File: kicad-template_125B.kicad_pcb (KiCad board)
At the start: 2 copper layers, 60 x 80 mm, 3 parts, among them J1 Barrel_Jack_Switch, J2 AudioJack_TRS, J3 AudioJack_TRS

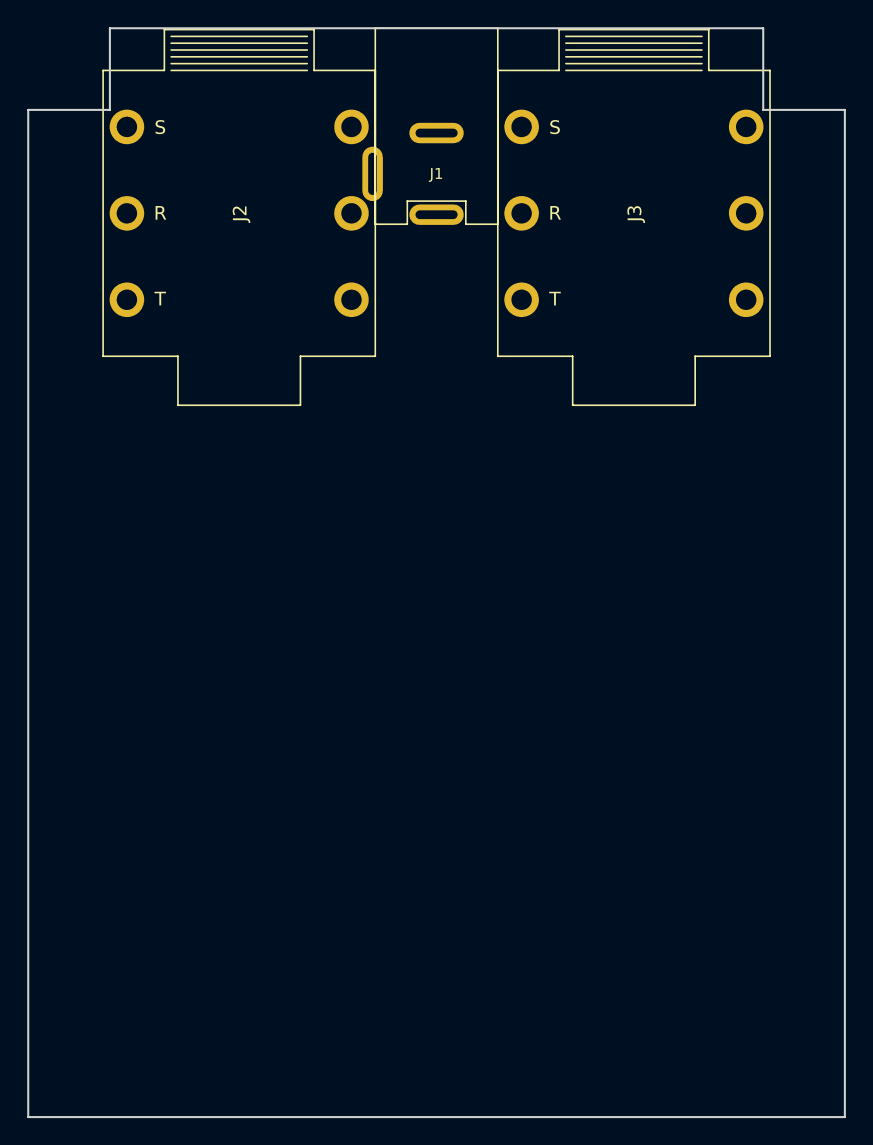
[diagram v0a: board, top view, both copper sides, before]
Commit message: Added jacks to schematic, filetted 125B PCB
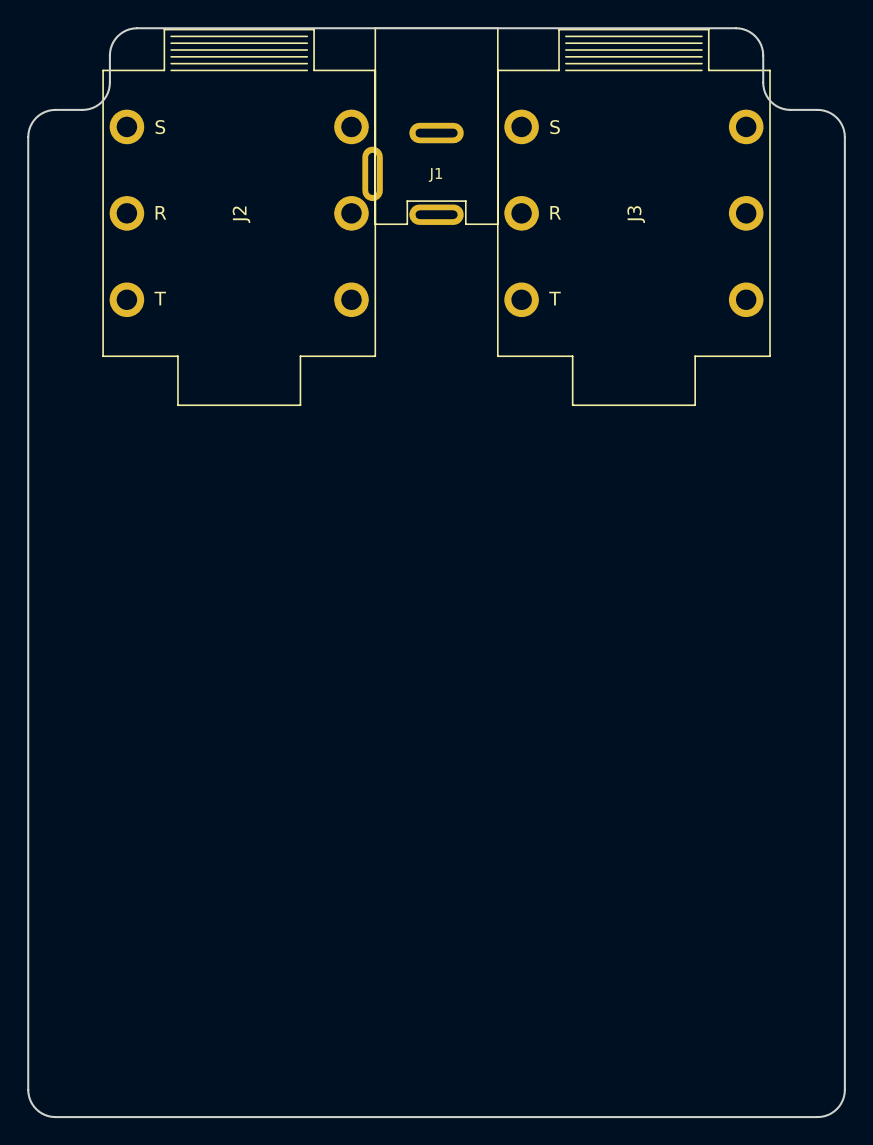
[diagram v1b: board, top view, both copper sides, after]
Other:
- outline, holes or cut-outs redrawn
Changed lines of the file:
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@@
   (general
     (thickness 1.6)
-    (drawings 36)
+    (drawings 44)
     (tracks 0)
     (zones 0)
@@
       (effects (font (size 1 1) (thickness 0.15)))
     )
+    (fp_line (start -2.15 12.7) (end -2.15 14.4) (layer F.SilkS) (width 0.12))
+    (fp_line (start 2.15 12.7) (end -2.15 12.7) (layer F.SilkS) (width 0.12))
+    (fp_line (start 2.15 14.4) (end 2.15 12.7) (layer F.SilkS) (width 0.12))
+    (fp_line (start 2.15 14.4) (end 4.5 14.4) (layer F.SilkS) (width 0.12))
+    (fp_line (start -4.5 0) (end -4.5 14.4) (layer F.SilkS) (width 0.12))
+    (fp_line (start -4.5 14.4) (end -2.15 14.4) (layer F.SilkS) (width 0.12))
+    (fp_line (start 4.5 0) (end 4.5 14.4) (layer F.SilkS) (width 0.12))
     (fp_line (start -4.5 0) (end 4.5 0) (layer F.SilkS) (width 0.12))
-    (fp_line (start 4.5 0) (end 4.5 14.4) (layer F.SilkS) (width 0.12))
-    (fp_line (start -4.5 14.4) (end -2.15 14.4) (layer F.SilkS) (width 0.12))
-    (fp_line (start -4.5 0) (end -4.5 14.4) (layer F.SilkS) (width 0.12))
-    (fp_line (start 2.15 14.4) (end 4.5 14.4) (layer F.SilkS) (width 0.12))
-    (fp_line (start 2.15 14.4) (end 2.15 12.7) (layer F.SilkS) (width 0.12))
-    (fp_line (start 2.15 12.7) (end -2.15 12.7) (layer F.SilkS) (width 0.12))
-    (fp_line (start -2.15 12.7) (end -2.15 14.4) (layer F.SilkS) (width 0.12))
     (pad 3 thru_hole oval (at -4.7 10.7 180) (size 1.5 4) (drill oval 0.65 3.1) (layers *.Cu *.Mask)
       (net 4 "Net-(J1-Pad3)"))
@@
       (effects (font (size 1 1) (thickness 0.15)))
     )
+    (fp_line (start 10 -10.5) (end 10 10.5) (layer F.SilkS) (width 0.12))
+    (fp_line (start -10 10.5) (end -10 -10.5) (layer F.SilkS) (width 0.12))
+    (fp_line (start -10 10.5) (end -4.5 10.5) (layer F.SilkS) (width 0.12))
+    (fp_line (start -4.5 10.5) (end -4.5 14.1) (layer F.SilkS) (width 0.12))
+    (fp_line (start -4.5 14.1) (end 4.5 14.1) (layer F.SilkS) (width 0.12))
+    (fp_line (start 4.5 14.1) (end 4.5 10.5) (layer F.SilkS) (width 0.12))
+    (fp_line (start 4.5 10.5) (end 10 10.5) (layer F.SilkS) (width 0.12))
+    (fp_line (start 10 -10.5) (end 5.5 -10.5) (layer F.SilkS) (width 0.12))
+    (fp_line (start 5.5 -10.5) (end 5.5 -13.5) (layer F.SilkS) (width 0.12))
+    (fp_line (start 5.5 -13.5) (end -5.5 -13.5) (layer F.SilkS) (width 0.12))
+    (fp_line (start -5.5 -13.5) (end -5.5 -10.5) (layer F.SilkS) (width 0.12))
+    (fp_line (start -5.5 -10.5) (end -10 -10.5) (layer F.SilkS) (width 0.12))
+    (fp_line (start -5 -13) (end 5 -13) (layer F.SilkS) (width 0.12))
+    (fp_line (start 5 -12.5) (end -5 -12.5) (layer F.SilkS) (width 0.12))
+    (fp_line (start -5 -12) (end 5 -12) (layer F.SilkS) (width 0.12))
+    (fp_line (start 5 -11.5) (end -5 -11.5) (layer F.SilkS) (width 0.12))
+    (fp_line (start -5 -11) (end 5 -11) (layer F.SilkS) (width 0.12))
     (fp_line (start 5 -10.5) (end -5 -10.5) (layer F.SilkS) (width 0.12))
-    (fp_line (start -5 -11) (end 5 -11) (layer F.SilkS) (width 0.12))
-    (fp_line (start 5 -11.5) (end -5 -11.5) (layer F.SilkS) (width 0.12))
-    (fp_line (start -5 -12) (end 5 -12) (layer F.SilkS) (width 0.12))
-    (fp_line (start 5 -12.5) (end -5 -12.5) (layer F.SilkS) (width 0.12))
-    (fp_line (start -5 -13) (end 5 -13) (layer F.SilkS) (width 0.12))
-    (fp_line (start -5.5 -10.5) (end -10 -10.5) (layer F.SilkS) (width 0.12))
-    (fp_line (start -5.5 -13.5) (end -5.5 -10.5) (layer F.SilkS) (width 0.12))
-    (fp_line (start 5.5 -13.5) (end -5.5 -13.5) (layer F.SilkS) (width 0.12))
-    (fp_line (start 5.5 -10.5) (end 5.5 -13.5) (layer F.SilkS) (width 0.12))
-    (fp_line (start 10 -10.5) (end 5.5 -10.5) (layer F.SilkS) (width 0.12))
-    (fp_line (start 4.5 10.5) (end 10 10.5) (layer F.SilkS) (width 0.12))
-    (fp_line (start 4.5 14.1) (end 4.5 10.5) (layer F.SilkS) (width 0.12))
-    (fp_line (start -4.5 14.1) (end 4.5 14.1) (layer F.SilkS) (width 0.12))
-    (fp_line (start -4.5 10.5) (end -4.5 14.1) (layer F.SilkS) (width 0.12))
-    (fp_line (start -10 10.5) (end -4.5 10.5) (layer F.SilkS) (width 0.12))
-    (fp_line (start -10 10.5) (end -10 -10.5) (layer F.SilkS) (width 0.12))
-    (fp_line (start 10 -10.5) (end 10 10.5) (layer F.SilkS) (width 0.12))
     (fp_text user R (at -5.8 0) (layer F.SilkS)
       (effects (font (size 1 1) (thickness 0.15)))
@@
       (effects (font (size 1 1) (thickness 0.15)))
     )
+    (fp_line (start 10 -10.5) (end 10 10.5) (layer F.SilkS) (width 0.12))
+    (fp_line (start -10 10.5) (end -10 -10.5) (layer F.SilkS) (width 0.12))
+    (fp_line (start -10 10.5) (end -4.5 10.5) (layer F.SilkS) (width 0.12))
+    (fp_line (start -4.5 10.5) (end -4.5 14.1) (layer F.SilkS) (width 0.12))
+    (fp_line (start -4.5 14.1) (end 4.5 14.1) (layer F.SilkS) (width 0.12))
+    (fp_line (start 4.5 14.1) (end 4.5 10.5) (layer F.SilkS) (width 0.12))
+    (fp_line (start 4.5 10.5) (end 10 10.5) (layer F.SilkS) (width 0.12))
+    (fp_line (start 10 -10.5) (end 5.5 -10.5) (layer F.SilkS) (width 0.12))
+    (fp_line (start 5.5 -10.5) (end 5.5 -13.5) (layer F.SilkS) (width 0.12))
+    (fp_line (start 5.5 -13.5) (end -5.5 -13.5) (layer F.SilkS) (width 0.12))
+    (fp_line (start -5.5 -13.5) (end -5.5 -10.5) (layer F.SilkS) (width 0.12))
+    (fp_line (start -5.5 -10.5) (end -10 -10.5) (layer F.SilkS) (width 0.12))
+    (fp_line (start -5 -13) (end 5 -13) (layer F.SilkS) (width 0.12))
+    (fp_line (start 5 -12.5) (end -5 -12.5) (layer F.SilkS) (width 0.12))
+    (fp_line (start -5 -12) (end 5 -12) (layer F.SilkS) (width 0.12))
+    (fp_line (start 5 -11.5) (end -5 -11.5) (layer F.SilkS) (width 0.12))
+    (fp_line (start -5 -11) (end 5 -11) (layer F.SilkS) (width 0.12))
     (fp_line (start 5 -10.5) (end -5 -10.5) (layer F.SilkS) (width 0.12))
-    (fp_line (start -5 -11) (end 5 -11) (layer F.SilkS) (width 0.12))
-    (fp_line (start 5 -11.5) (end -5 -11.5) (layer F.SilkS) (width 0.12))
-    (fp_line (start -5 -12) (end 5 -12) (layer F.SilkS) (width 0.12))
-    (fp_line (start 5 -12.5) (end -5 -12.5) (layer F.SilkS) (width 0.12))
-    (fp_line (start -5 -13) (end 5 -13) (layer F.SilkS) (width 0.12))
-    (fp_line (start -5.5 -10.5) (end -10 -10.5) (layer F.SilkS) (width 0.12))
-    (fp_line (start -5.5 -13.5) (end -5.5 -10.5) (layer F.SilkS) (width 0.12))
-    (fp_line (start 5.5 -13.5) (end -5.5 -13.5) (layer F.SilkS) (width 0.12))
-    (fp_line (start 5.5 -10.5) (end 5.5 -13.5) (layer F.SilkS) (width 0.12))
-    (fp_line (start 10 -10.5) (end 5.5 -10.5) (layer F.SilkS) (width 0.12))
-    (fp_line (start 4.5 10.5) (end 10 10.5) (layer F.SilkS) (width 0.12))
-    (fp_line (start 4.5 14.1) (end 4.5 10.5) (layer F.SilkS) (width 0.12))
-    (fp_line (start -4.5 14.1) (end 4.5 14.1) (layer F.SilkS) (width 0.12))
-    (fp_line (start -4.5 10.5) (end -4.5 14.1) (layer F.SilkS) (width 0.12))
-    (fp_line (start -10 10.5) (end -4.5 10.5) (layer F.SilkS) (width 0.12))
-    (fp_line (start -10 10.5) (end -10 -10.5) (layer F.SilkS) (width 0.12))
-    (fp_line (start 10 -10.5) (end 10 10.5) (layer F.SilkS) (width 0.12))
     (fp_text user R (at -5.8 0) (layer F.SilkS)
       (effects (font (size 1 1) (thickness 0.15)))
@@
     )
   )
+  (gr_arc (start -28 20.25) (end -30 20.25) (angle -90) (layer Edge.Cuts) (width 0.15))
+  (gr_arc (start 28 20.25) (end 28 22.25) (angle -90) (layer Edge.Cuts) (width 0.15))
+  (gr_arc (start 28 -49.75) (end 30 -49.75) (angle -90) (layer Edge.Cuts) (width 0.15))
+  (gr_arc (start 26 -53.75) (end 24 -53.75) (angle -90) (layer Edge.Cuts) (width 0.15))
+  (gr_arc (start 22 -55.75) (end 24 -55.75) (angle -90) (layer Edge.Cuts) (width 0.15))
+  (gr_arc (start -22 -55.75) (end -22 -57.75) (angle -90) (layer Edge.Cuts) (width 0.15))
+  (gr_arc (start -26 -53.75) (end -26 -51.75) (angle -90) (layer Edge.Cuts) (width 0.15))
+  (gr_arc (start -28 -49.75) (end -28 -51.75) (angle -90) (layer Edge.Cuts) (width 0.15))
   (gr_circle (center -27.75 -55) (end -25.75 -55) (layer Dwgs.User) (width 0.1))
   (gr_circle (center 27.75 -55) (end 29.75 -55) (layer Dwgs.User) (width 0.1))
@@
   (gr_arc (start 27.1491 55) (end 27.049103 60.599997) (angle -90.9999799) (layer Dwgs.User) (width 0.1))
   (gr_arc (start -27.45 55.3) (end -32.75 55.3) (angle -90) (layer Dwgs.User) (width 0.1))
-  (gr_line (start 24 -57.75) (end -24 -57.75) (layer Edge.Cuts) (width 0.15))
-  (gr_line (start 24 -51.75) (end 24 -57.75) (layer Edge.Cuts) (width 0.15))
-  (gr_line (start 30 -51.75) (end 24 -51.75) (layer Edge.Cuts) (width 0.15))
-  (gr_line (start 30 22.25) (end 30 -51.75) (layer Edge.Cuts) (width 0.15))
-  (gr_line (start -30 22.25) (end 30 22.25) (layer Edge.Cuts) (width 0.15))
-  (gr_line (start -30 -51.75) (end -30 22.25) (layer Edge.Cuts) (width 0.15))
-  (gr_line (start -24 -51.75) (end -30 -51.75) (layer Edge.Cuts) (width 0.15))
-  (gr_line (start -24 -57.75) (end -24 -51.75) (layer Edge.Cuts) (width 0.15))
+  (gr_line (start 22 -57.75) (end -22 -57.75) (layer Edge.Cuts) (width 0.15))
+  (gr_line (start 24 -53.75) (end 24 -55.75) (layer Edge.Cuts) (width 0.15))
+  (gr_line (start 28 -51.75) (end 26 -51.75) (layer Edge.Cuts) (width 0.15))
+  (gr_line (start 30 20.25) (end 30 -49.75) (layer Edge.Cuts) (width 0.15))
+  (gr_line (start -28 22.25) (end 28 22.25) (layer Edge.Cuts) (width 0.15))
+  (gr_line (start -30 -49.75) (end -30 20.25) (layer Edge.Cuts) (width 0.15))
+  (gr_line (start -26 -51.75) (end -28 -51.75) (layer Edge.Cuts) (width 0.15))
+  (gr_line (start -24 -55.75) (end -24 -53.75) (layer Edge.Cuts) (width 0.15))
 )
